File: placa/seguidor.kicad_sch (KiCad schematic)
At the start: 17 parts, among them J1 Conn_01x02_Pin, J2 Conn_01x15_Socket, SW1 btn_reset, SW2 btn_arranque, U1 ATmega328P-P, U2 LM7805_TO220, Y1 Crystal

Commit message: circuito modificado
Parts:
- removed C3: C, symbol Device:C
- removed SW1: btn_reset, symbol Switch:SW_Push
- added C7: C, symbol Device:C
- C1, C4: footprint (none) -> Capacitor_THT:C_Disc_D6.0mm_W2.5mm_P5.00mm
- C2: value 10u -> 47u; footprint (none) -> Capacitor_THT:CP_Radial_D5.0mm_P2.00mm
- C5, C6: footprint (none) -> Capacitor_THT:C_Disc_D5.0mm_W2.5mm_P5.00mm
- D1: footprint (none) -> LED_THT:LED_D4.0mm
- J2: footprint (none) -> Connector_PinSocket_2.54mm:PinSocket_1x15_P2.54mm_Horizontal
- R1: value 1k -> 10k
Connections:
- net +5V: now also J2.10 (Pin_10), J2.14 (Pin_14), J2.2 (Pin_2), J2.6 (Pin_6), U1.20 (AVCC), U1.7 (VCC); no longer U1.21 (AREF)
- net GND: now also C1.2, C4.2, J2.1 (Pin_1), J2.13 (Pin_13), J2.5 (Pin_5), J2.9 (Pin_9), C7.2
- net sensor2: now reaches J2.11 (Pin_11)
- net sensor1: now reaches J2.15 (Pin_15)
- net sensor4: now reaches J2.3 (Pin_3)
- net sensor3: now reaches J2.7 (Pin_7)
- new net: C7.1, U1.21 (AREF)
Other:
- moved on the sheet: C1, C4, R1

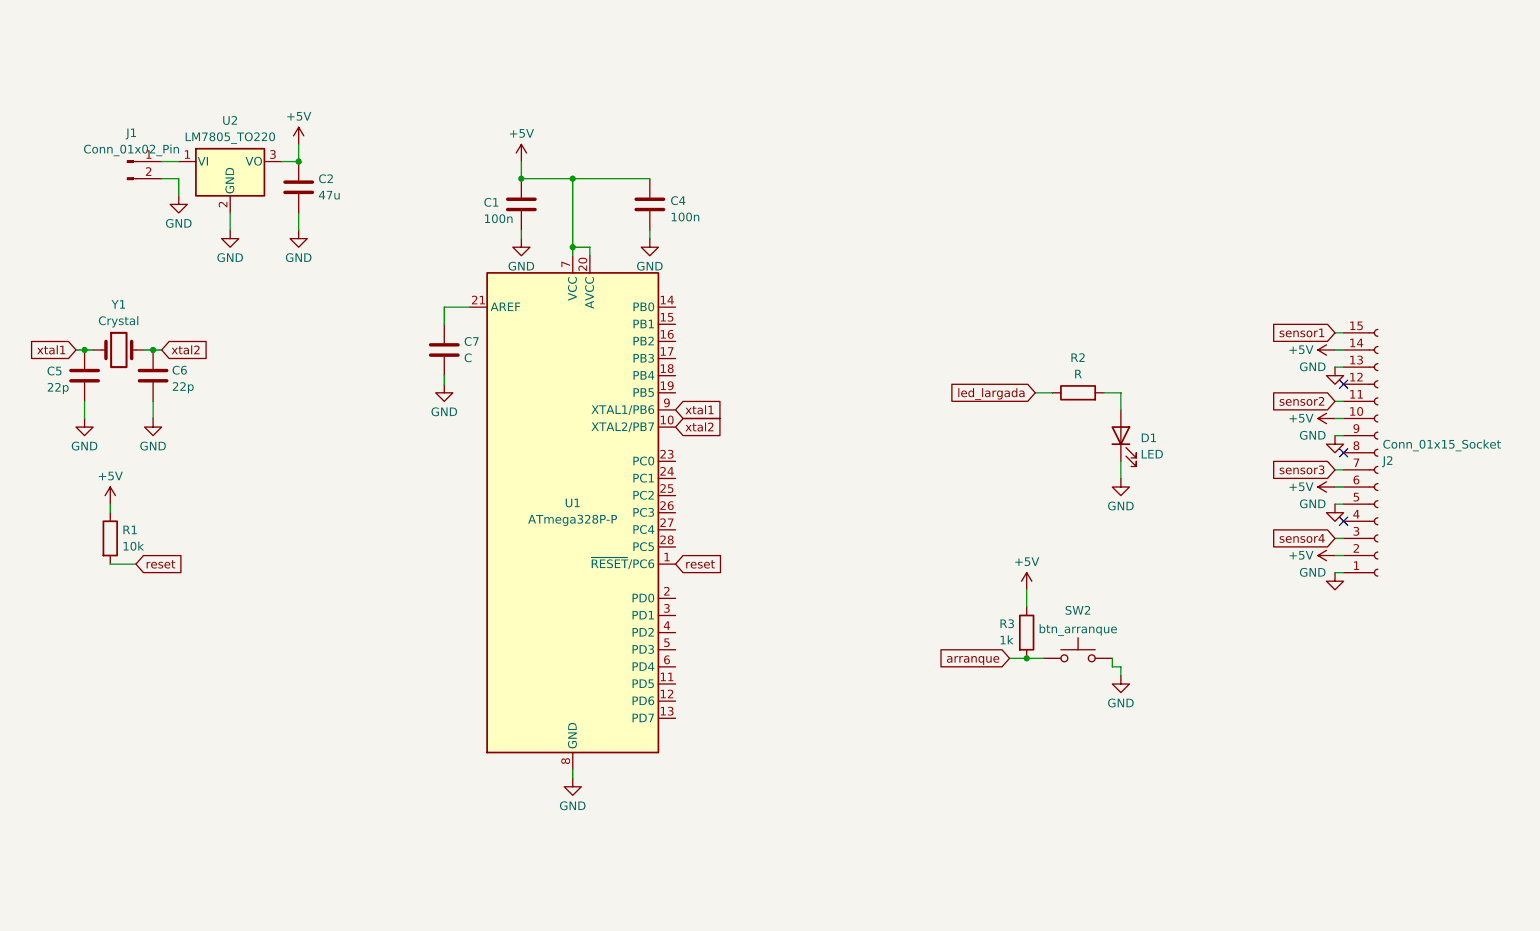
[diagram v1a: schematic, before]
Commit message: agregados componentes al pcb, faltan conectores
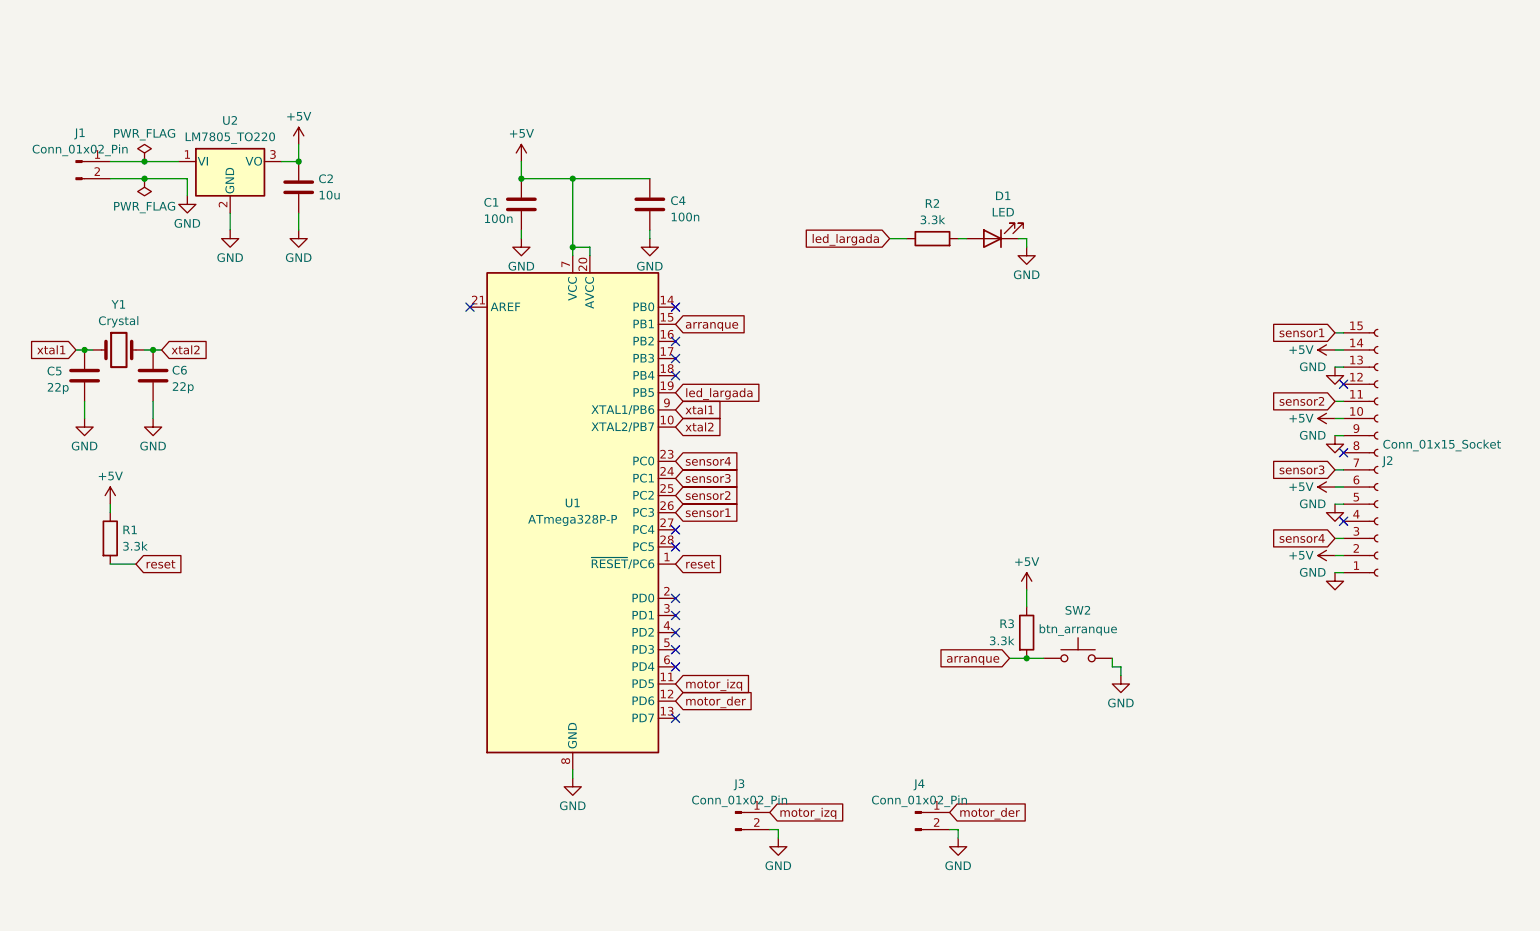
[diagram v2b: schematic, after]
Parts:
- removed C7: C, symbol Device:C
- added J3, J4: Conn_01x02_Pin, symbol Connector:Conn_01x02_Pin
- C2: value 47u -> 10u
- R1: value 10k -> 3.3k; footprint (none) -> Resistor_THT:R_Axial_DIN0204_L3.6mm_D1.6mm_P5.08mm_Horizontal
- R2: value R -> 3.3k; footprint (none) -> Resistor_THT:R_Axial_DIN0204_L3.6mm_D1.6mm_P5.08mm_Horizontal
- R3: value 1k -> 3.3k; footprint (none) -> Resistor_THT:R_Axial_DIN0204_L3.6mm_D1.6mm_P5.08mm_Horizontal
- SW2: footprint (none) -> Button_Switch_THT:SW_PUSH_6mm_H5mm
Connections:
- net GND: now also J3.2 (Pin_2), J4.2 (Pin_2)
- net arranque: now also U1.15 (PB1)
- net led_largada: now also U1.19 (PB5)
- net sensor1: now also U1.26 (PC3)
- net sensor2: now also U1.25 (PC2)
- net sensor3: now also U1.24 (PC1)
- net sensor4: now also U1.23 (PC0)
- net motor_izq: now reaches U1.11 (PD5)
- net motor_izq: now also J3.1 (Pin_1)
- net motor_der: now reaches U1.12 (PD6)
- net motor_der: now also J4.1 (Pin_1)
- no-connect marks 3 -> 16
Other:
- moved on the sheet: D1, J1, R2

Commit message: cambiados capacitores en la placa
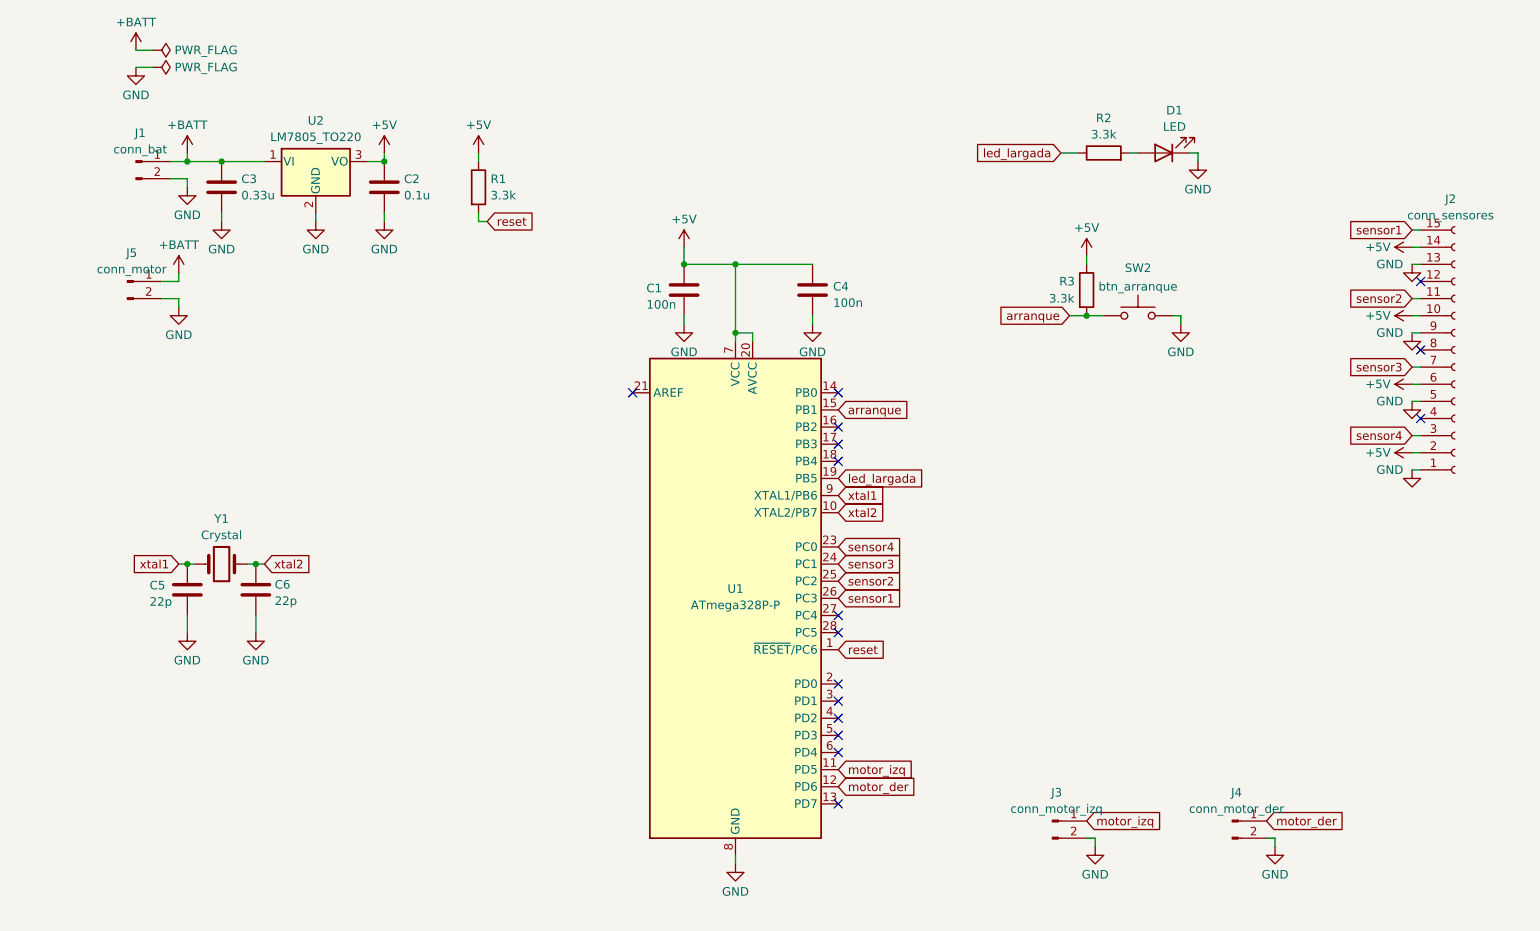
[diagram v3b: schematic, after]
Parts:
- added C3: 0.33u, Capacitor_THT:CP_Radial_D5.0mm_P2.00mm, symbol Device:C
- added J5: conn_motor, symbol Connector:Conn_01x02_Pin
- C2: value 10u -> 0.1u
- C5, C6: footprint Capacitor_THT:C_Disc_D5.0mm_W2.5mm_P5.00mm -> Capacitor_THT:C_Disc_D4.7mm_W2.5mm_P5.00mm
- J1: value Conn_01x02_Pin -> conn_bat
- J2: value Conn_01x15_Socket -> conn_sensores
- J3: value Conn_01x02_Pin -> conn_motor_izq
- J4: value Conn_01x02_Pin -> conn_motor_der
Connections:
- net GND: now also C3.2, J5.2 (Pin_2)
- net +BATT: now reaches J1.1 (Pin_1), U2.1 (VI)
- net +BATT: now also C3.1, J5.1 (Pin_1)
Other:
- moved on the sheet: C1, C2, C4, C5, C6, D1, J1, J2, J3, J4, R1, R2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

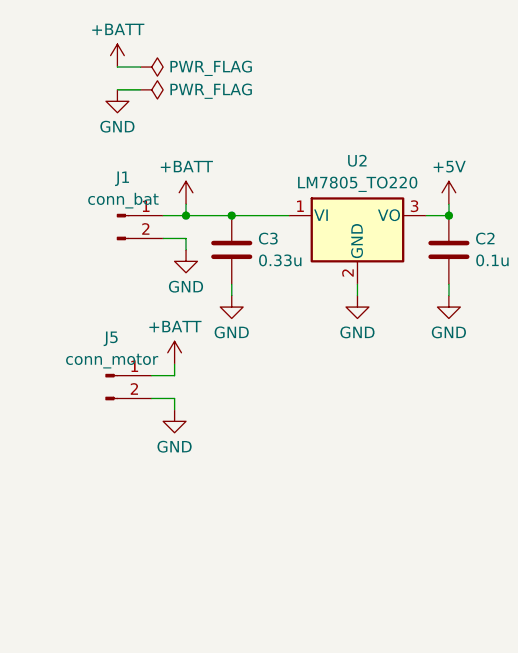
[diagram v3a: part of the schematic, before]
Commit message: conector de 3 pines para el puente H
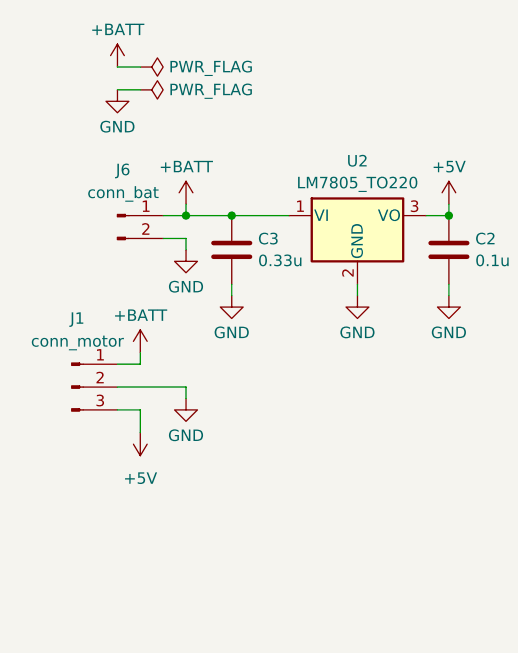
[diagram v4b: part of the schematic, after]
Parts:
- removed J1: conn_bat, symbol Connector:Conn_01x02_Pin
- removed J5: conn_motor, symbol Connector:Conn_01x02_Pin
- added J1: conn_motor, symbol Connector:Conn_01x03_Pin
- added J6: conn_bat, symbol Connector:Conn_01x02_Pin
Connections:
- net +5V: now also J1.3 (Pin_3)
- net +BATT: now also J1.1 (Pin_1), J6.1 (Pin_1)
- net GND: now also J1.2 (Pin_2), J6.2 (Pin_2)
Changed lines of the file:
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@@
 	(wire
 		(pts
+			(xy 41.91 57.15) (xy 44.45 57.15)
+		)
+		(stroke
+			(width 0)
+			(type default)
+		)
+	)
+	(wire
+		(pts
 			(xy 142.24 59.69) (xy 142.24 58.42)
 		)
@@
 	(wire
 		(pts
-			(xy 48.26 55.88) (xy 45.72 55.88)
+			(xy 133.35 60.96) (xy 130.81 60.96)
 		)
 		(stroke
@@
 	(wire
 		(pts
-			(xy 133.35 60.96) (xy 130.81 60.96)
+			(xy 44.45 52.07) (xy 44.45 50.8)
 		)
 		(stroke
@@
 	(wire
 		(pts
-			(xy 48.26 53.34) (xy 48.26 52.07)
+			(xy 41.91 21.59) (xy 44.45 21.59)
 		)
 		(stroke
@@
 	(wire
 		(pts
-			(xy 41.91 21.59) (xy 44.45 21.59)
+			(xy 231.14 81.28) (xy 232.41 81.28)
 		)
 		(stroke
@@
 	(wire
 		(pts
-			(xy 231.14 81.28) (xy 232.41 81.28)
+			(xy 41.91 54.61) (xy 49.53 54.61)
 		)
 		(stroke
@@
 	(wire
 		(pts
+			(xy 44.45 57.15) (xy 44.45 59.69)
+		)
+		(stroke
+			(width 0)
+			(type default)
+		)
+	)
+	(wire
+		(pts
 			(xy 49.53 35.56) (xy 54.61 35.56)
 		)
@@
 	(wire
 		(pts
-			(xy 45.72 53.34) (xy 48.26 53.34)
+			(xy 41.91 52.07) (xy 44.45 52.07)
 		)
 		(stroke
@@
 	(wire
 		(pts
-			(xy 48.26 57.15) (xy 48.26 55.88)
+			(xy 49.53 55.88) (xy 49.53 54.61)
 		)
 		(stroke
@@
 	(symbol
 		(lib_id "power:+BATT")
-		(at 48.26 52.07 0)
+		(at 44.45 50.8 0)
 		(unit 1)
 		(body_style 1)
@@
 		(fields_autoplaced yes)
 		(property "Reference" "#PWR027"
-			(at 48.26 55.88 0)
+			(at 44.45 54.61 0)
 			(hide yes)
 			(show_name no)
@@
 		)
 		(property "Value" "+BATT"
-			(at 48.26 47.9369 0)
+			(at 44.45 46.6669 0)
 			(show_name no)
 			(do_not_autoplace no)
@@
 		)
 		(property "Footprint" ""
-			(at 48.26 52.07 0)
+			(at 44.45 50.8 0)
 			(hide yes)
 			(show_name no)
@@
 		)
 		(property "Datasheet" ""
-			(at 48.26 52.07 0)
+			(at 44.45 50.8 0)
 			(hide yes)
 			(show_name no)
@@
 		)
 		(property "Description" "Power symbol creates a global label with name \"+BATT\""
-			(at 48.26 52.07 0)
+			(at 44.45 50.8 0)
 			(hide yes)
 			(show_name no)
@@
 	)
 	(symbol
+		(lib_id "power:+5V")
+		(at 44.45 59.69 180)
+		(unit 1)
+		(body_style 1)
+		(exclude_from_sim no)
+		(in_bom yes)
+		(on_board yes)
+		(in_pos_files yes)
+		(dnp no)
+		(fields_autoplaced yes)
+		(property "Reference" "#PWR031"
+			(at 44.45 55.88 0)
+			(hide yes)
+			(show_name no)
+			(do_not_autoplace no)
+			(effects
+				(font
+					(size 1.27 1.27)
+				)
+			)
+		)
+		(property "Value" "+5V"
+			(at 44.45 64.77 0)
+			(show_name no)
+			(do_not_autoplace no)
+			(effects
+				(font
+					(size 1.27 1.27)
+				)
+			)
+		)
+		(property "Footprint" ""
+			(at 44.45 59.69 0)
+			(hide yes)
+			(show_name no)
+			(do_not_autoplace no)
+			(effects
+				(font
+					(size 1.27 1.27)
+				)
+			)
+		)
+		(property "Datasheet" ""
+			(at 44.45 59.69 0)
+			(hide yes)
+			(show_name no)
+			(do_not_autoplace no)
+			(effects
+				(font
+					(size 1.27 1.27)
+				)
+			)
+		)
+		(property "Description" "Power symbol creates a global label with name \"+5V\""
+			(at 44.45 59.69 0)
+			(hide yes)
+			(show_name no)
+			(do_not_autoplace no)
+			(effects
+				(font
+					(size 1.27 1.27)
+				)
+			)
+		)
+		(pin "1"
+		)
+		(instances
+			(project "seguidor"
+				(path "/38da49ba-8049-40df-bae2-a6aa45c27be1"
+					(reference "#PWR031")
+					(unit 1)
+				)
+			)
+		)
+	)
+	(symbol
 		(lib_id "power:GND")
 		(at 59.69 105.41 0)
@@
 	)
 	(symbol
-		(lib_id "Connector:Conn_01x02_Pin")
-		(at 41.91 35.56 0)
+		(lib_id "Connector:Conn_01x03_Pin")
+		(at 36.83 54.61 0)
 		(unit 1)
 		(body_style 1)
@@
 		(fields_autoplaced yes)
 		(property "Reference" "J1"
-			(at 42.545 31.3393 0)
+			(at 37.465 46.99 0)
 			(show_name no)
 			(do_not_autoplace no)
@@
 			)
 		)
-		(property "Value" "conn_bat"
-			(at 42.545 33.7636 0)
+		(property "Value" "conn_motor"
+			(at 37.465 49.53 0)
 			(show_name no)
 			(do_not_autoplace no)
@@
 		)
 		(property "Footprint" ""
-			(at 41.91 35.56 0)
+			(at 36.83 54.61 0)
 			(hide yes)
 			(show_name no)
@@
 		)
 		(property "Datasheet" ""
-			(at 41.91 35.56 0)
+			(at 36.83 54.61 0)
 			(hide yes)
 			(show_name no)
@@
 			)
 		)
-		(property "Description" "Generic connector, single row, 01x02, script generated"
-			(at 41.91 35.56 0)
+		(property "Description" "Generic connector, single row, 01x03, script generated"
+			(at 36.83 54.61 0)
 			(hide yes)
 			(show_name no)
@@
 			)
 		)
-		(pin "1"
-		)
 		(pin "2"
 		)
-		(instances
-			(project "seguidor"
-				(path "/38da49ba-8049-40df-bae2-a6aa45c27be1"
-					(reference "J1")
-					(unit 1)
-				)
-			)
-		)
-	)
-	(symbol
-		(lib_id "Connector:Conn_01x02_Pin")
-		(at 40.64 53.34 0)
-		(unit 1)
-		(body_style 1)
-		(exclude_from_sim no)
-		(in_bom yes)
-		(on_board yes)
-		(in_pos_files yes)
-		(dnp no)
-		(fields_autoplaced yes)
-		(property "Reference" "J5"
-			(at 41.275 49.1193 0)
-			(show_name no)
-			(do_not_autoplace no)
-			(effects
-				(font
-					(size 1.27 1.27)
-				)
-			)
-		)
-		(property "Value" "conn_motor"
-			(at 41.275 51.5436 0)
-			(show_name no)
-			(do_not_autoplace no)
-			(effects
-				(font
-					(size 1.27 1.27)
-				)
-			)
-		)
-		(property "Footprint" ""
-			(at 40.64 53.34 0)
-			(hide yes)
-			(show_name no)
-			(do_not_autoplace no)
-			(effects
-				(font
-					(size 1.27 1.27)
-				)
-			)
-		)
-		(property "Datasheet" ""
-			(at 40.64 53.34 0)
-			(hide yes)
-			(show_name no)
-			(do_not_autoplace no)
-			(effects
-				(font
-					(size 1.27 1.27)
-				)
-			)
-		)
-		(property "Description" "Generic connector, single row, 01x02, script generated"
-			(at 40.64 53.34 0)
-			(hide yes)
-			(show_name no)
-			(do_not_autoplace no)
-			(effects
-				(font
-					(size 1.27 1.27)
-				)
-			)
-		)
 		(pin "1"
 		)
-		(pin "2"
+		(pin "3"
 		)
 		(instances
 			(project "seguidor"
 				(path "/38da49ba-8049-40df-bae2-a6aa45c27be1"
-					(reference "J5")
+					(reference "J1")
 					(unit 1)
 				)
@@
 	)
 	(symbol
+		(lib_id "Connector:Conn_01x02_Pin")
+		(at 41.91 35.56 0)
+		(unit 1)
+		(body_style 1)
+		(exclude_from_sim no)
+		(in_bom yes)
+		(on_board yes)
+		(in_pos_files yes)
+		(dnp no)
+		(fields_autoplaced yes)
+		(property "Reference" "J6"
+			(at 42.545 30.48 0)
+			(show_name no)
+			(do_not_autoplace no)
+			(effects
+				(font
+					(size 1.27 1.27)
+				)
+			)
+		)
+		(property "Value" "conn_bat"
+			(at 42.545 33.02 0)
+			(show_name no)
+			(do_not_autoplace no)
+			(effects
+				(font
+					(size 1.27 1.27)
+				)
+			)
+		)
+		(property "Footprint" ""
+			(at 41.91 35.56 0)
+			(hide yes)
+			(show_name no)
+			(do_not_autoplace no)
+			(effects
+				(font
+					(size 1.27 1.27)
+				)
+			)
+		)
+		(property "Datasheet" ""
+			(at 41.91 35.56 0)
+			(hide yes)
+			(show_name no)
+			(do_not_autoplace no)
+			(effects
+				(font
+					(size 1.27 1.27)
+				)
+			)
+		)
+		(property "Description" "Generic connector, single row, 01x02, script generated"
+			(at 41.91 35.56 0)
+			(hide yes)
+			(show_name no)
+			(do_not_autoplace no)
+			(effects
+				(font
+					(size 1.27 1.27)
+				)
+			)
+		)
+		(pin "1"
+		)
+		(pin "2"
+		)
+		(instances
+			(project "seguidor"
+				(path "/38da49ba-8049-40df-bae2-a6aa45c27be1"
+					(reference "J6")
+					(unit 1)
+				)
+			)
+		)
+	)
+	(symbol
 		(lib_id "power:PWR_FLAG")
 		(at 44.45 19.05 270)
@@
 	(symbol
 		(lib_id "power:GND")
-		(at 48.26 57.15 0)
+		(at 49.53 55.88 0)
 		(unit 1)
 		(body_style 1)
@@
 		(fields_autoplaced yes)
 		(property "Reference" "#PWR025"
-			(at 48.26 63.5 0)
+			(at 49.53 62.23 0)
 			(hide yes)
 			(show_name no)
@@
 		)
 		(property "Value" "GND"
-			(at 48.26 61.2831 0)
+			(at 49.53 60.0131 0)
 			(show_name no)
 			(do_not_autoplace no)
@@
 		)
 		(property "Footprint" ""
-			(at 48.26 57.15 0)
+			(at 49.53 55.88 0)
 			(hide yes)
 			(show_name no)
@@
 		)
 		(property "Datasheet" ""
-			(at 48.26 57.15 0)
+			(at 49.53 55.88 0)
 			(hide yes)
 			(show_name no)
@@
 		)
 		(property "Description" "Power symbol creates a global label with name \"GND\" , ground"
-			(at 48.26 57.15 0)
+			(at 49.53 55.88 0)
 			(hide yes)
 			(show_name no)
